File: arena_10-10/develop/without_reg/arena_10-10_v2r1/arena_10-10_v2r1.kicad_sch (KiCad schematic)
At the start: 0 parts

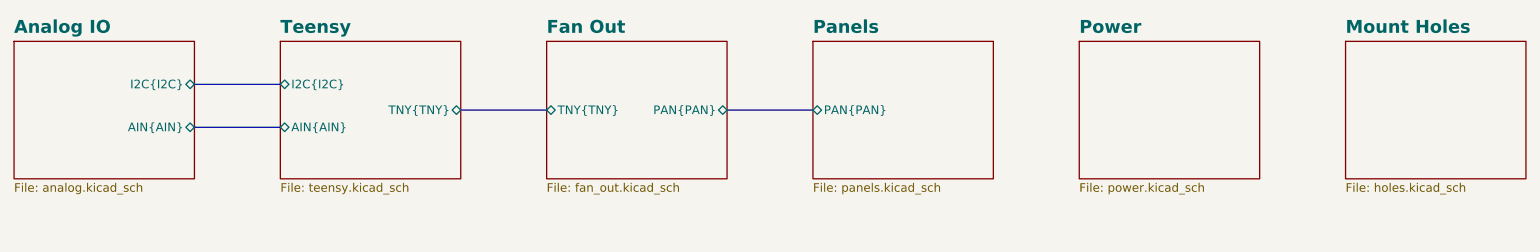
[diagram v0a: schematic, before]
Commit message: Added clamp to IMON.  Connected PG and IMON to teensy.
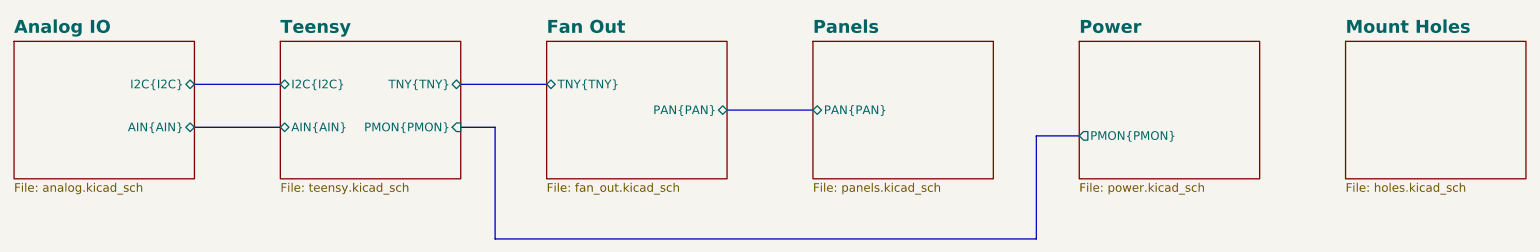
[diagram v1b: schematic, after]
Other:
- sheet Power ports: added PMON{PMON}; removed none
- sheet Teensy ports: added PMON{PMON}; removed none
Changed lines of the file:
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@@
+	(bus
+		(pts
+			(xy 186.69 64.77) (xy 186.69 49.53)
+		)
+		(stroke
+			(width 0)
+			(type default)
+		)
+	)
 	(bus
 		(pts
@@
 	(bus
 		(pts
-			(xy 101.6 45.72) (xy 114.3 45.72)
+			(xy 101.6 48.26) (xy 106.68 48.26)
+		)
+		(stroke
+			(width 0)
+			(type default)
+		)
+	)
+	(bus
+		(pts
+			(xy 106.68 64.77) (xy 186.69 64.77)
+		)
+		(stroke
+			(width 0)
+			(type default)
+		)
+	)
+	(bus
+		(pts
+			(xy 106.68 48.26) (xy 106.68 64.77)
+		)
+		(stroke
+			(width 0)
+			(type default)
+		)
+	)
+	(bus
+		(pts
+			(xy 101.6 41.91) (xy 114.3 41.91)
 		)
 		(stroke
@@
 		(pts
 			(xy 140.97 45.72) (xy 153.67 45.72)
+		)
+		(stroke
+			(width 0)
+			(type default)
+		)
+	)
+	(bus
+		(pts
+			(xy 186.69 49.53) (xy 193.04 49.53)
 		)
 		(stroke
@@
 		)
 		(pin "TNY{TNY}" bidirectional
-			(at 114.3 45.72 180)
+			(at 114.3 41.91 180)
 			(effects
 				(font
@@
 		)
 		(pin "TNY{TNY}" bidirectional
-			(at 101.6 45.72 0)
+			(at 101.6 41.91 0)
 			(effects
 				(font
@@
 				)
 				(justify left)
+			)
+		)
+		(pin "PMON{PMON}" input
+			(at 101.6 48.26 0)
+			(effects
+				(font
+					(size 1.27 1.27)
+				)
+				(justify right)
 			)
 		)
@@
 			)
 		)
+		(pin "PMON{PMON}" output
+			(at 193.04 49.53 180)
+			(effects
+				(font
+					(size 1.27 1.27)
+				)
+				(justify left)
+			)
+		)
